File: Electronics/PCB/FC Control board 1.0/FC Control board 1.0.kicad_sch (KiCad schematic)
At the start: 3 parts

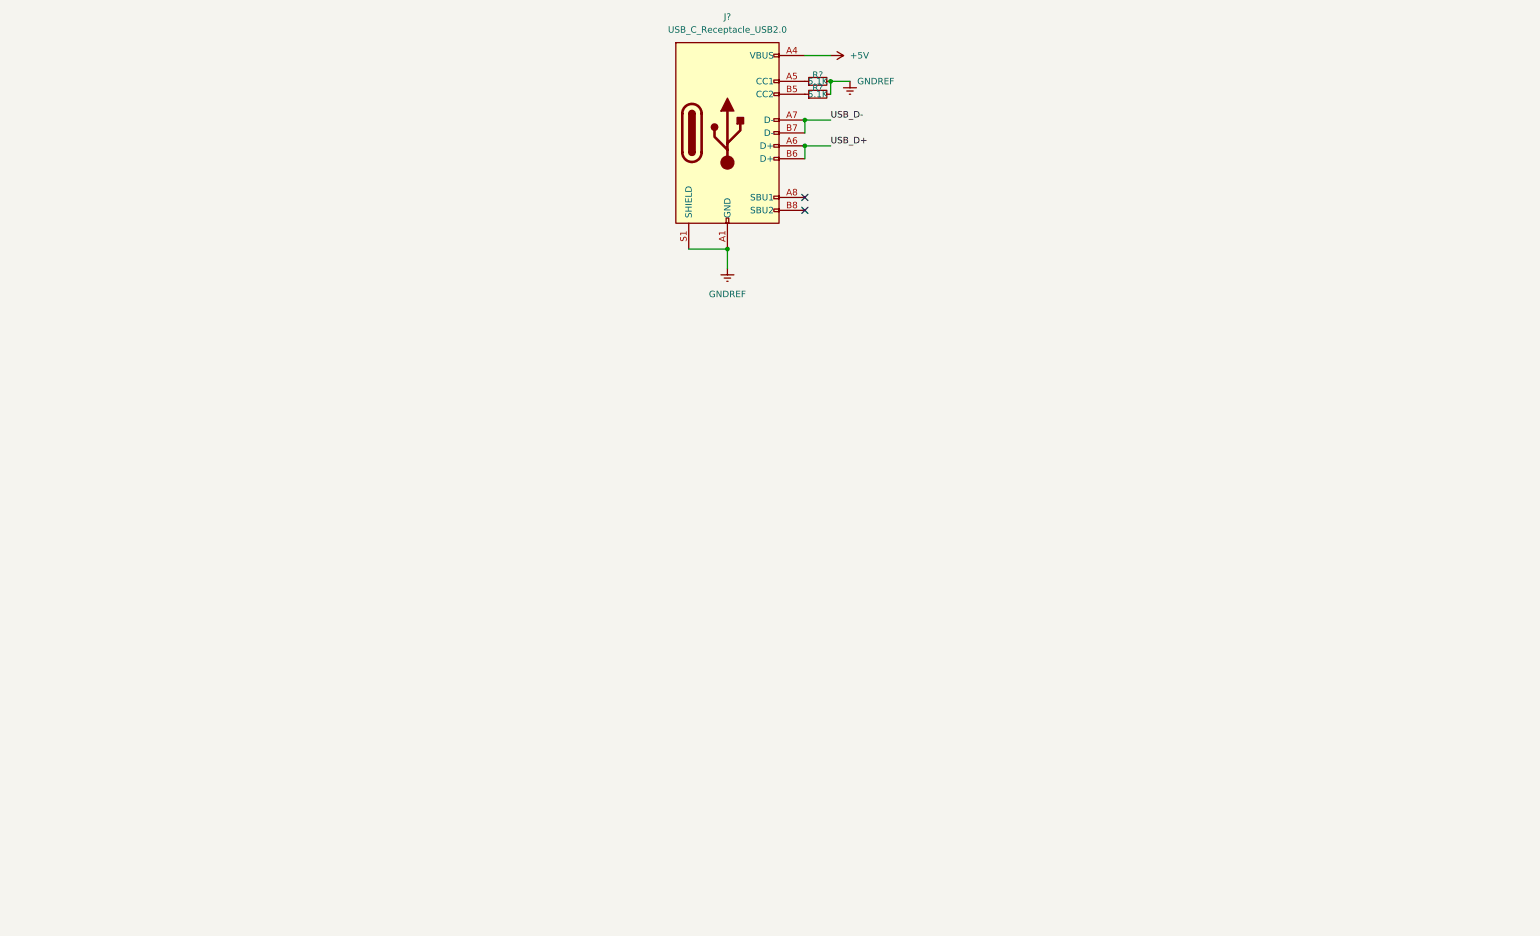
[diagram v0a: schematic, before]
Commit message: Begin electric motor control design
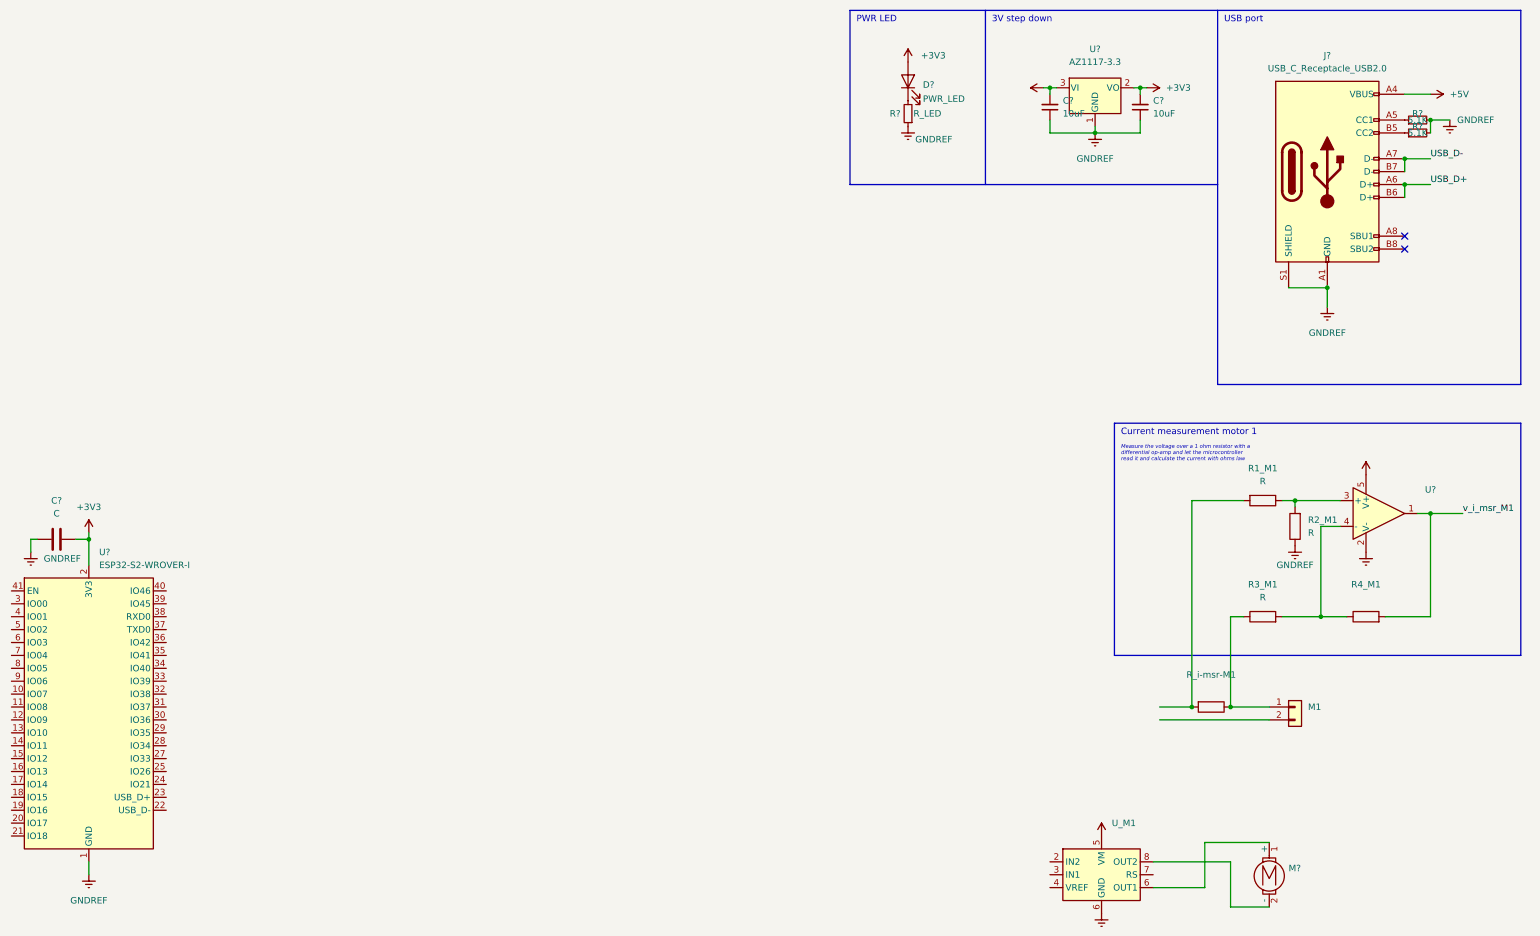
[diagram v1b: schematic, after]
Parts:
- added C? (x2): 10uF, Capacitor_SMD:C_1206_3216Metric, symbol Device:C_Small
- added C?: C, symbol Device:C
- added D?: PWR_LED, LED_SMD:LED_0805_2012Metric_Pad1.15x1.40mm_HandSolder, symbol Device:LED
- added M1: (no value), symbol Connector_Generic:Conn_01x02
- added M?: (no value), symbol Motor:Motor_DC_ALT
- added R1_M1, R2_M1, R3_M1: R, symbol Device:R
- added R4_M1, R_i-msr-M1: (no value), symbol Device:R
- added R?: R_LED, Resistor_SMD:R_0805_2012Metric_Pad1.20x1.40mm_HandSolder, symbol Device:R_Small
- added U?: ESP32-S2-WROVER-I, RF_Module:ESP32-S2-WROVER, symbol RF_Module:ESP32-S2-WROVER-I
- added U?: AZ1117-3.3, Package_TO_SOT_SMD:SOT-223-3_TabPin2, symbol Regulator_Linear:AZ1117-3.3
- added U?: (no value), symbol pspice:OPAMP
- added U_M1: (no value), Package_SO:HSOP-8-1EP_3.9x4.9mm_P1.27mm_EP2.41x3.1mm, symbol Driver_LED:LED5000
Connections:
- net GNDREF: now also C?.1, C?.1, C?.1, R2_M1.1, R?.1, U?.1 (GND), U?.1 (GND), U?.2 (V-), U?.26 (GND), U?.42 (GND), U?.43 (GND), U_M1.6 (OUT1), U_M1.9 (GND)
- new net: M?.1 (+), U_M1.6 (OUT1)
- new net: M?.2 (-), U_M1.8 (OUT2)
- new net: R3_M1.2, R4_M1.1, U?.4 (-)
- new net: R1_M1.1, R2_M1.2, U?.3 (+)
- new net: M1.1 (Pin_1), R3_M1.1, R_i-msr-M1.1
- new net: R1_M1.2, R_i-msr-M1.2
- new net: D?.1 (K), R?.2
- new net +3V3: C?.2, C?.2, D?.2 (A), U?.2 (3V3), U?.2 (VO)
- new net VCC: C?.2, U?.3 (VI), U?.5 (V+), U_M1.5 (VM)
- new net v_i_msr_M1: R4_M1.2, U?.1
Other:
- note added: "3V step down"
- note added: "Current measurement motor 1"
- note added: "Measure the voltage over a 1 ohm resistor with a differential op-amp and let the microcontroller read it and calculate the current with ohms law"
- note added: "PWR LED"
- note added: "USB port"
- moved on the sheet: J?, R?

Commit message: Continue PCB-design
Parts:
- removed U?: ESP32-S2-WROVER-I, RF_Module:ESP32-S2-WROVER, symbol RF_Module:ESP32-S2-WROVER-I
- removed U_M1: (no value), Package_SO:HSOP-8-1EP_3.9x4.9mm_P1.27mm_EP2.41x3.1mm, symbol Driver_LED:LED5000
- added BT1: (no value), symbol Device:Battery
- added C4: 100n, Capacitor_SMD:C_0805_2012Metric_Pad1.18x1.45mm_HandSolder, symbol Device:C_Small
- added R4: 10K, Resistor_SMD:R_0805_2012Metric_Pad1.20x1.40mm_HandSolder, symbol Device:R_Small
- added SW1: RESET, Button_Switch_SMD:SW_Push_1P1T_NO_6x6mm_H9.5mm, symbol Switch:SW_Push
- added SW2: BOOT, Button_Switch_SMD:SW_Push_1P1T_NO_6x6mm_H9.5mm, symbol Switch:SW_Push
- added U1: (no value), symbol FC_library:ESP32-S3-WROOM-1-N8
- added U4: (no value), symbol RF:NRF24L01_Breakout
- added U_M1: (no value), symbol FC_library:TB67H451AFNG,EL
- M1: value (none) -> Conn_01x02
- M2: renamed from M?; value (none) -> Motor_DC_ALT
- R4_M1: value (none) -> R
- R_i-msr-M1: value (none) -> 1; footprint (none) -> Resistor_SMD:R_2512_6332Metric_Pad1.40x3.35mm_HandSolder
- U3: renamed from U?; value (none) -> TS321; footprint (none) -> Package_TO_SOT_SMD:SOT-23-5_HandSoldering
- gave numbers to parts that had none: 9
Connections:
- net +3V3: now also R4.2, U1.2 (3V3), U4.2 (VCC), U_M1.5 (VM)
- net GNDREF: now also BT1.2 (-), C4.1, SW1.1, SW2.1, U1.1 (GND), U1.40 (GND), U1.41 (GND), U4.1 (GND), U_M1.1 (GND)
- net VCC: now also BT1.1 (+)
- net at M2.1 (+): now also U_M1.6 (OUT1)
- net at M2.2 (-): now also U_M1.8 (OUT2)
- new net EN: C4.2, R4.1, SW1.2, U1.3 (EN)
- new net IO0: SW2.2, U1.27 (IO0)
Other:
- note added: "Boot"
- note added: "ESP reset"
- moved on the sheet: C1

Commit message: Restart project
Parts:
- removed M1: Conn_01x02, symbol Connector_Generic:Conn_01x02
- removed R1_M1, R2_M1, R3_M1, R4_M1: R, symbol Device:R
- removed R_i-msr-M1: 1, Resistor_SMD:R_2512_6332Metric_Pad1.40x3.35mm_HandSolder, symbol Device:R
- removed U3: TS321, Package_TO_SOT_SMD:SOT-23-5_HandSoldering, symbol pspice:OPAMP
- added BZ1: Buzzer1, Buzzer_Beeper:Buzzer_12x9.5RM7.6, symbol Device:Buzzer
- added BZ2: Buzzer2, Buzzer_Beeper:Buzzer_12x9.5RM7.6, symbol Device:Buzzer
- added BZ3: Buzzer3, Buzzer_Beeper:Buzzer_12x9.5RM7.6, symbol Device:Buzzer
- added C7 (x2), C8 (x2): 10uF, Capacitor_SMD:C_1206_3216Metric, symbol Device:C_Small
- added C9: 10u, symbol Device:C
- added R10, R12, R5, R7: 5k, symbol Device:R
- added R11, R6, R8, R9: 10k, symbol Device:R
- added R_bat1: 80k, symbol Device:R
- added R_bat2: 50k, symbol Device:R
- added SW3: SW_SPST, symbol Switch:SW_SPST
- added U4: AZ1117-5.0, Package_TO_SOT_SMD:TO-252-2, symbol Regulator_Linear:AZ1117-5.0
- added U5: LM358DRG3 2_4, Package_SO:SOIC-8_3.9x4.9mm_P1.27mm, symbol Device:Opamp_Dual
- added U6: LM358DRG3 1_3, Package_SO:SOIC-8_3.9x4.9mm_P1.27mm, symbol Device:Opamp_Dual
- added U7: AZ1117-3.3, Package_TO_SOT_SMD:SOT-223-3_TabPin2, symbol Regulator_Linear:AZ1117-3.3
- added Volume1: R_Buzzer, Potentiometer_THT:Potentiometer_Alps_RK09K_Single_Horizontal, symbol Device:R_Potentiometer
- BT1: value (none) -> Battery; footprint (none) -> Connector_JST:JST_EH_B2B-EH-A_1x02_P2.50mm_Vertical
- U1: value (none) -> ESP32-S3-WROOM-1-N8; footprint (none) -> FC_footprint_library:ESP32-S3-WROOM-1-N8
- U4: value (none) -> NRF24L01_Breakout; footprint (none) -> RF_Module:nRF24L01_Breakout
- U_M1: value (none) -> TB67H451AFNG,EL; footprint (none) -> Package_SO:HSOP-8-1EP_3.9x4.9mm_P1.27mm_EP2.41x3.1mm
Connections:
- net +3V3: now also C8.2, C9.2, U7.2 (VO), Volume1.1, Volume1.2; no longer U_M1.5 (VM)
- net +5V: now also C7.2, C8.2, U4.2 (VO), U7.3 (VI)
- net GNDREF: now also BZ1.2 (+), BZ2.2 (+), BZ3.2 (+), C7.1, C7.1, C8.1, C8.1, C9.1, R11.2, R6.2, R8.2, R9.2, R_bat2.2, SW3.1 (A), U4.1 (GND), U5.4 (V-), U6.4 (V-), U7.1 (GND); no longer BT1.2 (-)
- net USB_D+: now also U1.14 (IO20)
- net USB_D-: now also U1.13 (IO19)
- net VCC: now also U_M1.5 (VM), C7.2, R_bat1.1, U4.3 (VI), U5.8 (V+), U6.8 (V+)
- net at M2.1 (+): now also U_M1.8 (OUT2); no longer U_M1.6 (OUT1)
- net at M2.2 (-): now also U_M1.6 (OUT1); no longer U_M1.8 (OUT2)
- net M1_1: now reaches U_M1.2 (IN2)
- net M1_2: now reaches U_M1.3 (IN1)
- net CE: now reaches U4.3 (CE)
- net CE: now also U1.6 (IO6)
- net CSN: now reaches U4.4 (~{CSN})
- net CSN: now also U1.5 (IO5)
- net SCK: now reaches U4.5 (SCK)
- net SCK: now also U1.20 (IO12)
- net MOSI: now reaches U4.6 (MOSI)
- net MOSI: now also U1.19 (IO11)
- net MISO: now reaches U4.7 (MISO)
- net MISO: now also U1.21 (IO13)
- net SDA: now reaches U1.12 (IO8)
- net SCL: now reaches U1.17 (IO9)
- net SS: now reaches U1.18 (IO10)
- net M1_ref_3V: now reaches U1.28 (IO35)
- net M1_ref_3V: now also U6.5 (+)
- net M2_ref_3V: now reaches U1.29 (IO36)
- net M2_ref_3V: now also U5.3 (+)
- net M3_ref_3V: now reaches U1.30 (IO37)
- net M3_ref_3V: now also U5.5 (+)
- net M4_ref_3V: now reaches U1.31 (IO38)
- net M4_ref_3V: now also U6.3 (+)
- net bat_level: now reaches U1.4 (IO4)
- net bat_level: now also R_bat1.2, R_bat2.1
- net Volume_pot: now reaches U1.7 (IO7)
- net Volume_pot: now also Volume1.3
- net Servo: now reaches U1.8 (IO15)
- new net: BT1.2 (-), SW3.2 (B)
- new net: R7.2, R8.1, U5.2 (-)
- new net: R5.2, R6.1, U6.2 (-)
- new net: R11.1, R12.2, U5.6 (-)
- new net: R10.2, R9.1, U6.6 (-)
- new net BUZZER_PIN: BZ1.1 (-)
- new net BUZZER_PIN2: BZ2.1 (-)
- new net BUZZER_PIN3: BZ3.1 (-)
- new net M1_ref_5V: R10.1, U6.7
- new net M2_ref_5V: U5.1
- new net M3_ref_5V: R12.1, U5.7
- new net M4_ref_5V: R5.1, U6.1
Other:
- note added: "3V step down (from USB 5V)"
- note added: "5V step down"
- note added: "Backup nRF24L01 if ESP-NOW/Bluetooth does not work"
- note added: "Battery measurement 8.4V -> 3.231V after divider"
- note added: "Buzzers"
- note added: "Reference signal boost from [0, 3.3]V to [0, 5.0]V"
- note removed: "Current measurement motor 1"
- note removed: "Measure the voltage over a 1 ohm resistor with a differential op-amp and let the microcontroller read it and calculate the current with ohms law"
- moved on the sheet: BT1, C1, D1, M2, R1, U1, U4, U_M1
